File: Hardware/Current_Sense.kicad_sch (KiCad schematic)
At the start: 32 parts, among them IC1 INA241A4IDR, IC2 AMC1350DWVR, IC3 TLV9002QDRQ1, J6 Scrut Conn, SW3 Scrut Select, U11 REF35125QDBVR

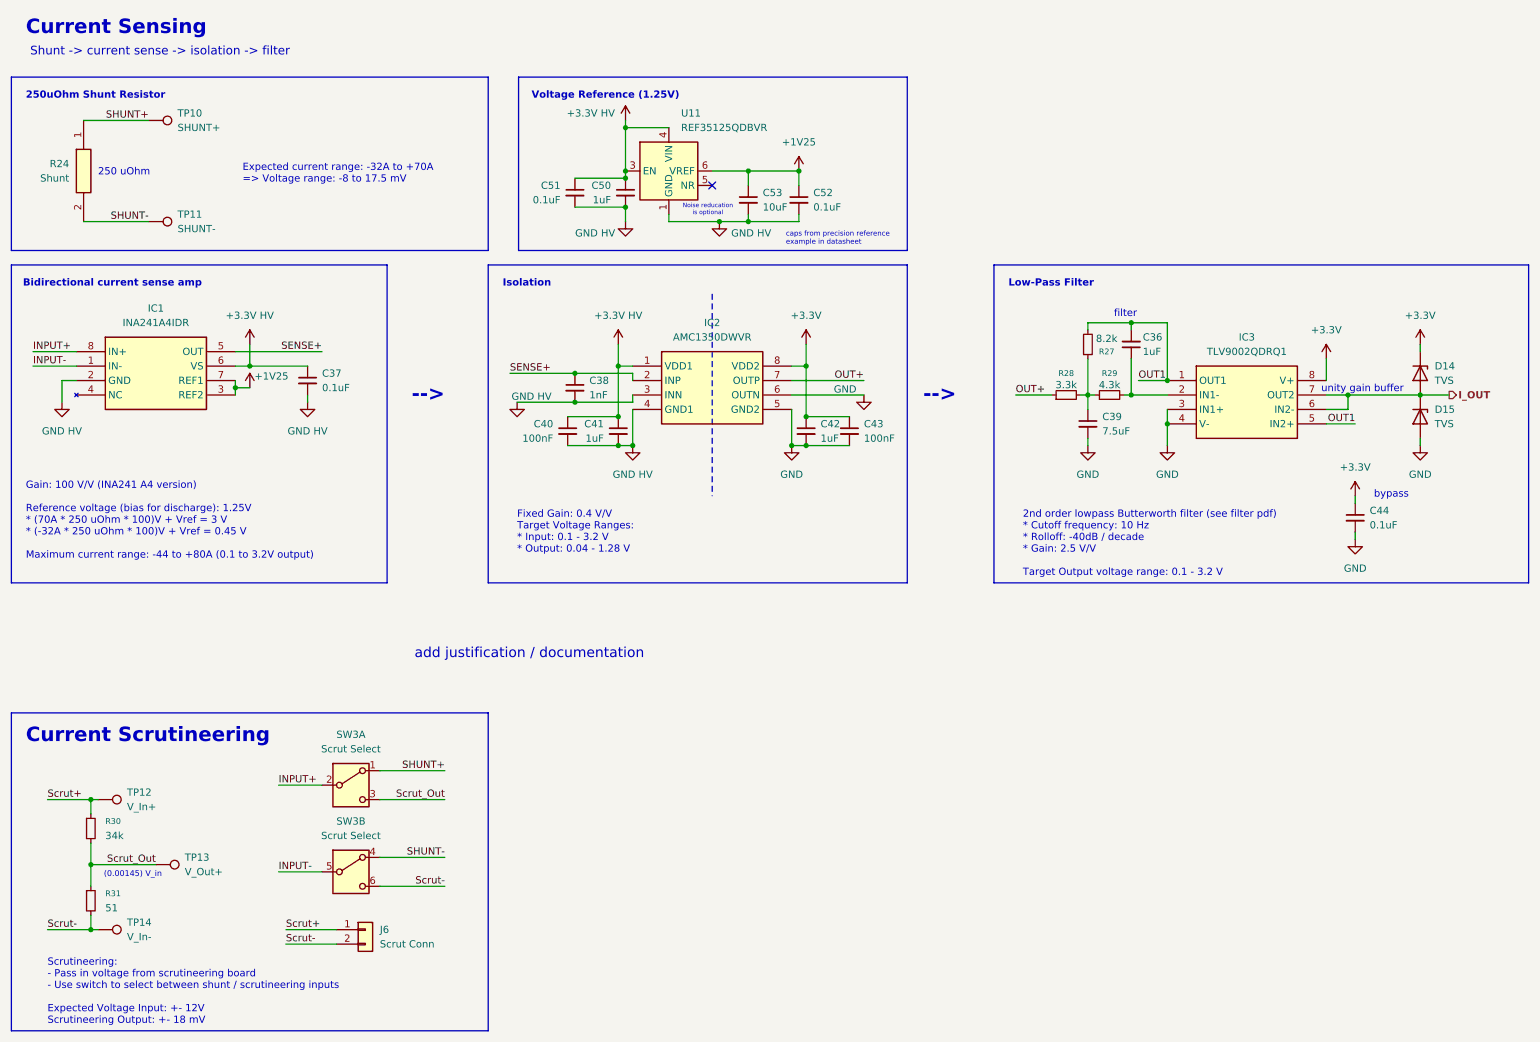
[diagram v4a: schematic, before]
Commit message: added vertical usb c
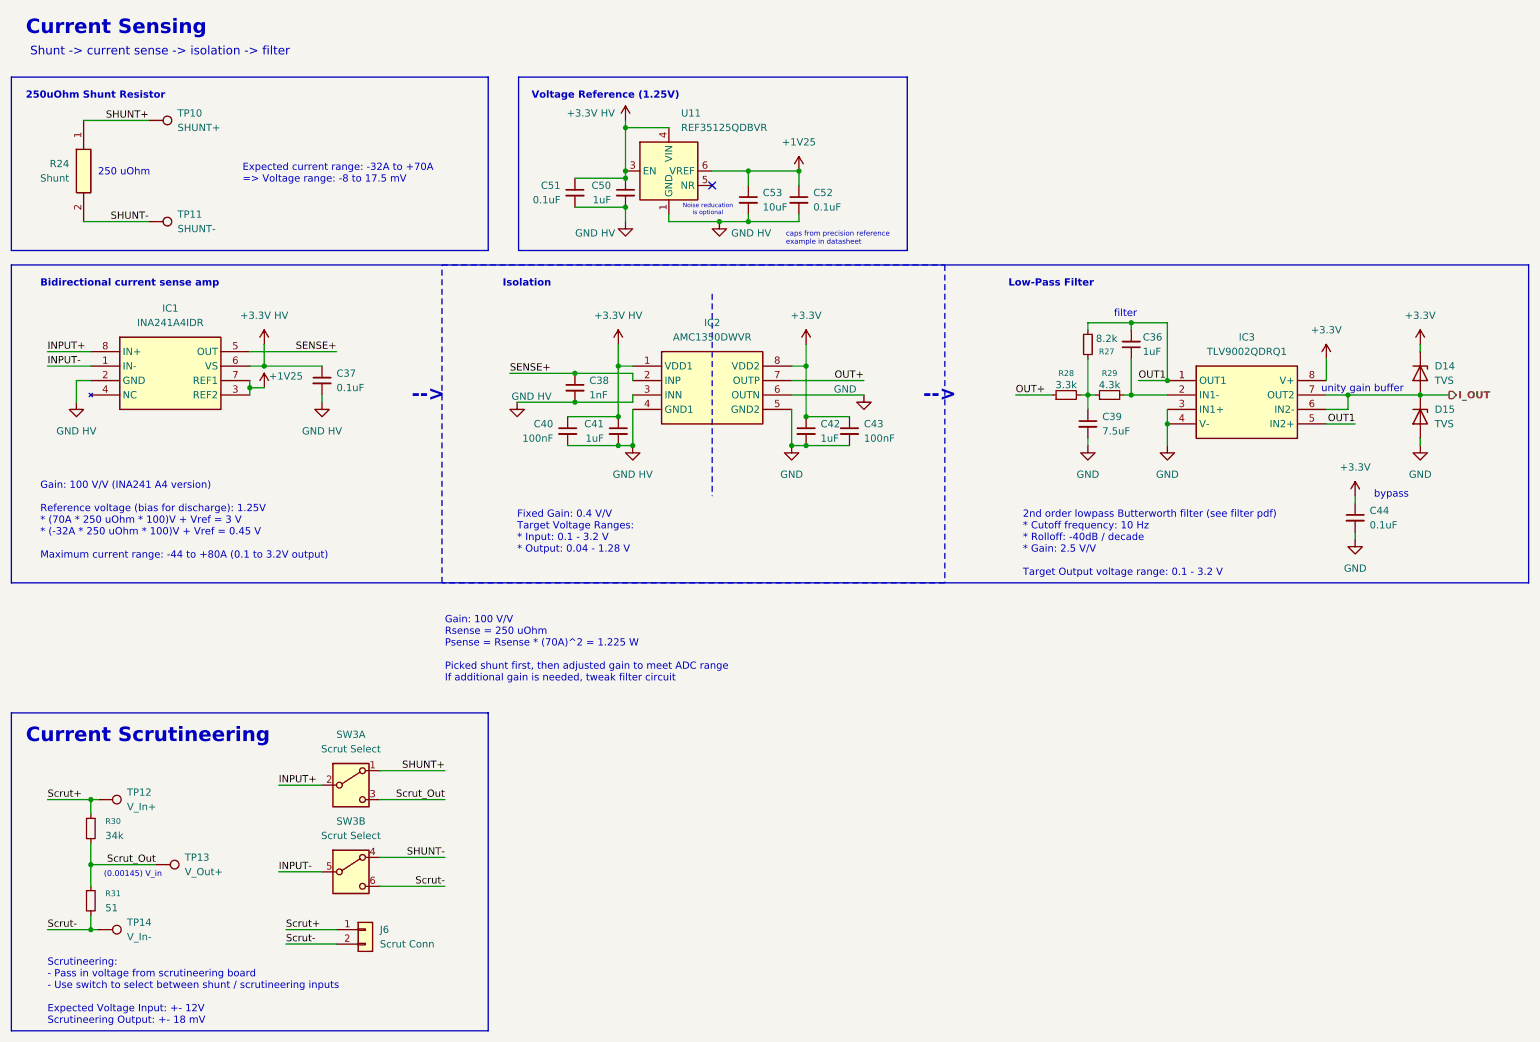
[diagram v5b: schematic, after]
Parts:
- R24: footprint WSBS8518L2500JK -> Parts:WSBS8518L2500JK
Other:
- note added: "Gain: 100 V/V Rsense = 250 uOhm Psense = Rsense * (70A)^2 = 1.225 W Picked shunt first, then adjusted gain to meet ADC range If additional gain is needed, tweak filter circuit"
- note removed: "add justification / documentation"
- moved on the sheet: C37, IC1

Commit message: lay out lay out
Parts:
- C39: renamed from C53; footprint Capacitor_SMD:C_0603_1608Metric_Pad1.08x0.95mm_HandSolder -> Capacitor_SMD:C_0805_2012Metric_Pad1.18x1.45mm_HandSolder; P/N (none) -> GRM21BR61H106KE43K
- IC2: renamed from IC1; footprint SOIC127P600X175-8N -> Parts:INA241A5IDR
- IC4: renamed from IC3; footprint SOIC127P600X175-8N -> Parts:TLV9002QDRQ1
- J6: footprint Connector_Molex:Molex_Micro-Fit_3.0_43650-0200_1x02_P3.00mm_Horizontal -> Connector_Molex:Molex_Nano-Fit_105309-xx02_1x02_P2.50mm_Vertical
- SW3: footprint (none) -> Button_Switch_SMD:SW_DPDT_CK_JS202011JCQN
- TP10, TP11, TP12, TP13, TP14: footprint (none) -> TestPoint:TestPoint_Pad_1.0x1.0mm
- renumbered C51 to C37, C50 to C38, C52 to C40, C36 to C41, C37 to C42, C38 to C43, C39 to C44, C40 to C45, C41 to C46, C42 to C47, C43 to C48, C44 to C49, D14 to D15, D15 to D16, IC2 to IC3, R27 to R25, R28 to R26, R29 to R27, R30 to R28, R31 to R29, U11 to U9
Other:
- moved on the sheet: C40

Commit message: changed shunt model, moved around folders; initial layout, routing soon
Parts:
- removed R24: Shunt, Parts:WSBS8518L2500JK, symbol WSBS8518L2500JK:WSBS8518L2500JK
- added R39: WSBS8518L2500JTP3, WSBS8518L2500JKM4, symbol WSBS8518L2500JKM4:WSBS8518L2500JKM4
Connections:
- net SHUNT+: now also R39.1
- net SHUNT-: now also R39.2
- no-connect marks 1 -> 3
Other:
- note added: "Footprint is M4 version; edit it to have M3 holes"
- moved on the sheet: TP10, TP11
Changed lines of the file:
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@@
 		)
 	)
-	(text "250 uOhm"
+	(text "250 \nuOhm"
 		(exclude_from_sim no)
-		(at 35.052 44.704 0)
+		(at 28.448 46.482 0)
 		(effects
 			(font
 				(size 1.27 1.27)
+				(thickness 0.254)
+				(bold yes)
 			)
 		)
@@
 	(text "Expected current range: -32A to +70A\n=> Voltage range: -8 to 17.5 mV"
 		(exclude_from_sim no)
-		(at 55.88 43.18 0)
+		(at 56.896 32.258 0)
 		(effects
 			(font
@@
 		)
 	)
+	(text "Footprint is M4 version; edit it to have M3 holes"
+		(exclude_from_sim no)
+		(at 17.78 55.88 0)
+		(effects
+			(font
+				(size 1.27 1.27)
+				(color 255 8 29 1)
+			)
+			(justify left top)
+		)
+	)
 	(junction
 		(at 29.21 154.94)
@@
 		(at 138.43 46.99)
 	)
+	(no_connect
+		(at 40.64 43.18)
+	)
+	(no_connect
+		(at 40.64 50.8)
+	)
 	(wire
 		(pts
@@
 	(wire
 		(pts
-			(xy 27.94 35.56) (xy 39.37 35.56)
+			(xy 40.64 45.72) (xy 50.8 45.72)
 		)
 		(stroke
@@
 	(wire
 		(pts
-			(xy 27.94 53.34) (xy 39.37 53.34)
+			(xy 40.64 48.26) (xy 50.8 48.26)
 		)
 		(stroke
@@
 	)
 	(label "SHUNT-"
-		(at 39.37 53.34 180)
+		(at 50.8 48.26 180)
 		(effects
 			(font
@@
 	)
 	(label "SHUNT+"
-		(at 39.37 35.56 180)
+		(at 50.8 45.72 180)
 		(effects
 			(font
@@
 	)
 	(symbol
+		(lib_id "WSBS8518L2500JKM4:WSBS8518L2500JKM4")
+		(at 40.64 43.18 0)
+		(mirror y)
+		(unit 1)
+		(exclude_from_sim no)
+		(in_bom yes)
+		(on_board yes)
+		(dnp no)
+		(fields_autoplaced yes)
+		(property "Reference" "R39"
+			(at 29.21 35.56 0)
+			(effects
+				(font
+					(size 1.27 1.27)
+				)
+			)
+		)
+		(property "Value" "WSBS8518L2500JTP3"
+			(at 29.21 38.1 0)
+			(effects
+				(font
+					(size 1.27 1.27)
+				)
+			)
+		)
+		(property "Footprint" "WSBS8518L2500JKM4"
+			(at 21.59 138.1 0)
+			(effects
+				(font
+					(size 1.27 1.27)
+				)
+				(justify left top)
+				(hide yes)
+			)
+		)
+		(property "Datasheet" "https://www.vishay.com/docs/30392/wsbs8518p3.pdf"
+			(at 21.59 238.1 0)
+			(effects
+				(font
+					(size 1.27 1.27)
+				)
+				(justify left top)
+				(hide yes)
+			)
+		)
+		(property "Description" "Power Metal Strip Battery Shunt Resistor With M4 Tapped Holes Very Low Value (50 u, 100 u, 125 u, and 250 u)"
+			(at 40.64 43.18 0)
+			(effects
+				(font
+					(size 1.27 1.27)
+				)
+				(hide yes)
+			)
+		)
+		(property "Height" "3"
+			(at 21.59 438.1 0)
+			(effects
+				(font
+					(size 1.27 1.27)
+				)
+				(justify left top)
+				(hide yes)
+			)
+		)
+		(property "Mouser Part Number" "71-WSBS8518L2500JTP3"
+			(at 21.59 538.1 0)
+			(effects
+				(font
+					(size 1.27 1.27)
+				)
+				(justify left top)
+				(hide yes)
+			)
+		)
+		(property "Mouser Price/Stock" "https://www.mouser.co.uk/ProductDetail/Vishay-Dale/WSBS8518L2500JKM4?qs=BZBei1rCqCBDT%2FHsm0OnWA%3D%3D"
+			(at 21.59 638.1 0)
+			(effects
+				(font
+					(size 1.27 1.27)
+				)
+				(justify left top)
+				(hide yes)
+			)
+		)
+		(property "Manufacturer_Name" "Vishay"
+			(at 21.59 738.1 0)
+			(effects
+				(font
+					(size 1.27 1.27)
+				)
+				(justify left top)
+				(hide yes)
+			)
+		)
+		(property "Manufacturer_Part_Number" "WSBS8518L2500JTP3"
+			(at 21.59 838.1 0)
+			(effects
+				(font
+					(size 1.27 1.27)
+				)
+				(justify left top)
+				(hide yes)
+			)
+		)
+		(pin "1"
+		)
+		(pin "MH2"
+		)
+		(pin "MH1"
+		)
+		(pin "2"
+		)
+		(instances
+			(project ""
+				(path "/a452d214-ea00-440d-a445-5d6103fda43a/7e38ba4d-a54c-4f69-a074-7d0a3dae713a"
+					(reference "R39")
+					(unit 1)
+				)
+			)
+		)
+	)
+	(symbol
 		(lib_id "Device:C_Small")
 		(at 114.3 82.55 0)
@@
 	(symbol
 		(lib_id "Connector:TestPoint")
-		(at 39.37 35.56 270)
+		(at 50.8 45.72 0)
 		(unit 1)
 		(exclude_from_sim no)
@@
 		(fields_autoplaced yes)
 		(property "Reference" "TP10"
-			(at 44.45 34.2899 90)
+			(at 53.34 41.1479 0)
 			(effects
 				(font
@@
 		)
 		(property "Value" "SHUNT+"
-			(at 44.45 36.8299 90)
+			(at 53.34 43.6879 0)
 			(effects
 				(font
@@
 		)
 		(property "Footprint" "TestPoint:TestPoint_Pad_1.0x1.0mm"
-			(at 39.37 40.64 0)
+			(at 55.88 45.72 0)
 			(effects
 				(font
@@
 		)
 		(property "Datasheet" "~"
-			(at 39.37 40.64 0)
+			(at 55.88 45.72 0)
 			(effects
 				(font
@@
 		)
 		(property "Description" "test point"
-			(at 39.37 35.56 0)
+			(at 50.8 45.72 0)
 			(effects
 				(font
@@
 	)
 	(symbol
-		(lib_id "WSBS8518L2500JK:WSBS8518L2500JK")
-		(at 27.94 35.56 90)
-		(mirror x)
-		(unit 1)
-		(exclude_from_sim no)
-		(in_bom yes)
-		(on_board yes)
-		(dnp no)
-		(property "Reference" "R24"
-			(at 25.4 43.1799 90)
-			(effects
-				(font
-					(size 1.27 1.27)
-				)
-				(justify left)
-			)
-		)
-		(property "Value" "Shunt"
-			(at 25.4 45.7199 90)
-			(effects
-				(font
-					(size 1.27 1.27)
-				)
-				(justify left)
-			)
-		)
-		(property "Footprint" "Parts:WSBS8518L2500JK"
-			(at 124.13 49.53 0)
-			(effects
-				(font
-					(size 1.27 1.27)
-				)
-				(justify left top)
-				(hide yes)
-			)
-		)
-		(property "Datasheet" "https://www.vishay.com/docs/30134/wsbs8518.pdf"
-			(at 224.13 49.53 0)
-			(effects
-				(font
-					(size 1.27 1.27)
-				)
-				(justify left top)
-				(hide yes)
-			)
-		)
-		(property "Description" "Current Sense Resistors - Through Hole 36watt 250 micro-ohm 5% Battery Shunt"
-			(at 27.94 35.56 0)
-			(effects
-				(font
-					(size 1.27 1.27)
-				)
-				(hide yes)
-			)
-		)
-		(property "Height" "3.1"
-			(at 424.13 49.53 0)
-			(effects
-				(font
-					(size 1.27 1.27)
-				)
-				(justify left top)
-				(hide yes)
-			)
-		)
-		(property "Mouser Part Number" "71-WSBS8518L2500JK"
-			(at 524.13 49.53 0)
-			(effects
-				(font
-					(size 1.27 1.27)
-				)
-				(justify left top)
-				(hide yes)
-			)
-		)
-		(property "Mouser Price/Stock" "https://www.mouser.co.uk/ProductDetail/Vishay-Dale/WSBS8518L2500JK?qs=i2mp%2Fn9EmlJ0b%2F4LBxCPeA%3D%3D"
-			(at 624.13 49.53 0)
-			(effects
-				(font
-					(size 1.27 1.27)
-				)
-				(justify left top)
-				(hide yes)
-			)
-		)
-		(property "Manufacturer_Name" "Vishay"
-			(at 724.13 49.53 0)
-			(effects
-				(font
-					(size 1.27 1.27)
-				)
-				(justify left top)
-				(hide yes)
-			)
-		)
-		(property "Manufacturer_Part_Number" "WSBS8518L2500JK"
-			(at 824.13 49.53 0)
-			(effects
-				(font
-					(size 1.27 1.27)
-				)
-				(justify left top)
-				(hide yes)
-			)
-		)
-		(pin "1"
-		)
-		(pin "2"
-		)
-		(instances
-			(project ""
-				(path "/a452d214-ea00-440d-a445-5d6103fda43a/7e38ba4d-a54c-4f69-a074-7d0a3dae713a"
-					(reference "R24")
-					(unit 1)
-				)
-			)
-		)
-	)
-	(symbol
 		(lib_id "Device:C_Small")
 		(at 154.94 90.17 0)
@@
 	(symbol
 		(lib_id "Connector:TestPoint")
-		(at 39.37 53.34 270)
+		(at 50.8 48.26 180)
 		(unit 1)
 		(exclude_from_sim no)
@@
 		(fields_autoplaced yes)
 		(property "Reference" "TP11"
-			(at 44.45 52.0699 90)
+			(at 53.34 50.2919 0)
 			(effects
 				(font
 					(size 1.27 1.27)
 				)
-				(justify left)
+				(justify right)
 			)
 		)
 		(property "Value" "SHUNT-"
-			(at 44.45 54.6099 90)
+			(at 53.34 52.8319 0)
 			(effects
 				(font
 					(size 1.27 1.27)
 				)
-				(justify left)
+				(justify right)
 			)
 		)
 		(property "Footprint" "TestPoint:TestPoint_Pad_1.0x1.0mm"
-			(at 39.37 58.42 0)
+			(at 45.72 48.26 0)
 			(effects
 				(font
@@
 		)
 		(property "Datasheet" "~"
-			(at 39.37 58.42 0)
+			(at 45.72 48.26 0)
 			(effects
 				(font
@@
 		)
 		(property "Description" "test point"
-			(at 39.37 53.34 0)
+			(at 50.8 48.26 0)
 			(effects
 				(font

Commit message: 9/20 workday: some layout stuff ye ye
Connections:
- net SHUNT+: now also R39.2; no longer R39.1
- net SHUNT-: now also R39.1; no longer R39.2
- net Battery_GND: now reaches R39.MH1
- net Output_GND: now reaches R39.MH2
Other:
- note added: "Low-Side Shunt: * Discharge: Output_GND -> Battery_GND * Charge: Battery_GND -> Output_GND"
- moved on the sheet: C37, C38, C39, C40, R39, TP10, TP11, U9
